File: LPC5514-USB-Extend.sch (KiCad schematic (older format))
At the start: 5 parts

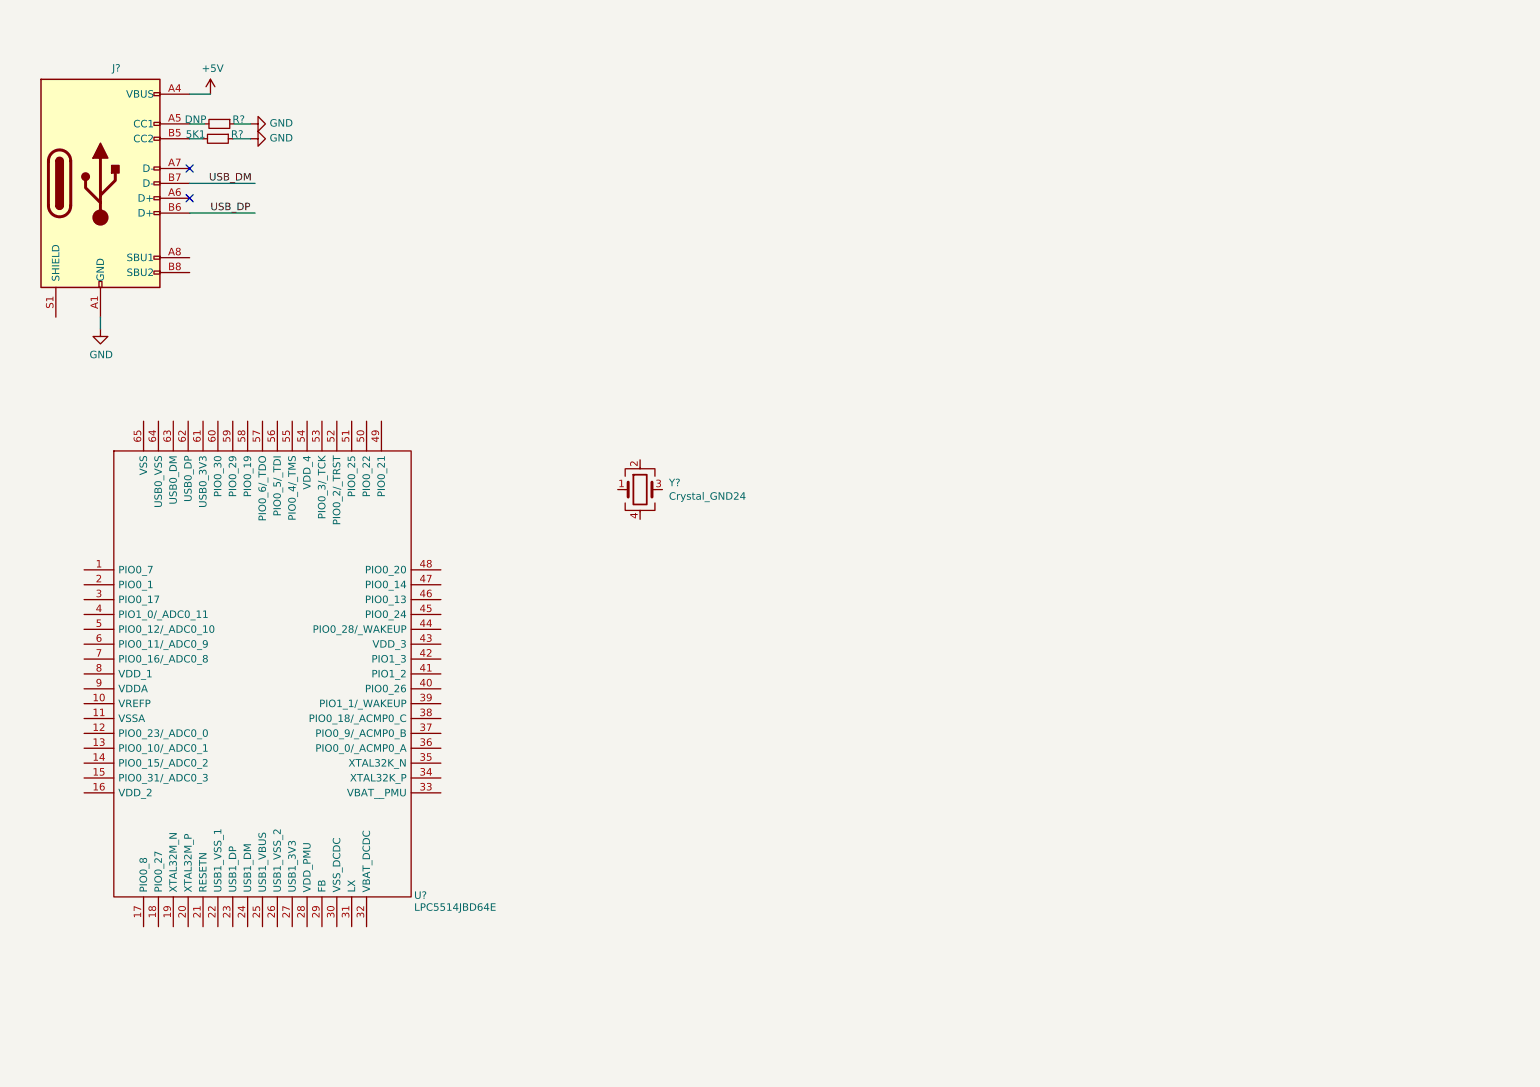
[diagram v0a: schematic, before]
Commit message: update design, usb0/1 connection & power
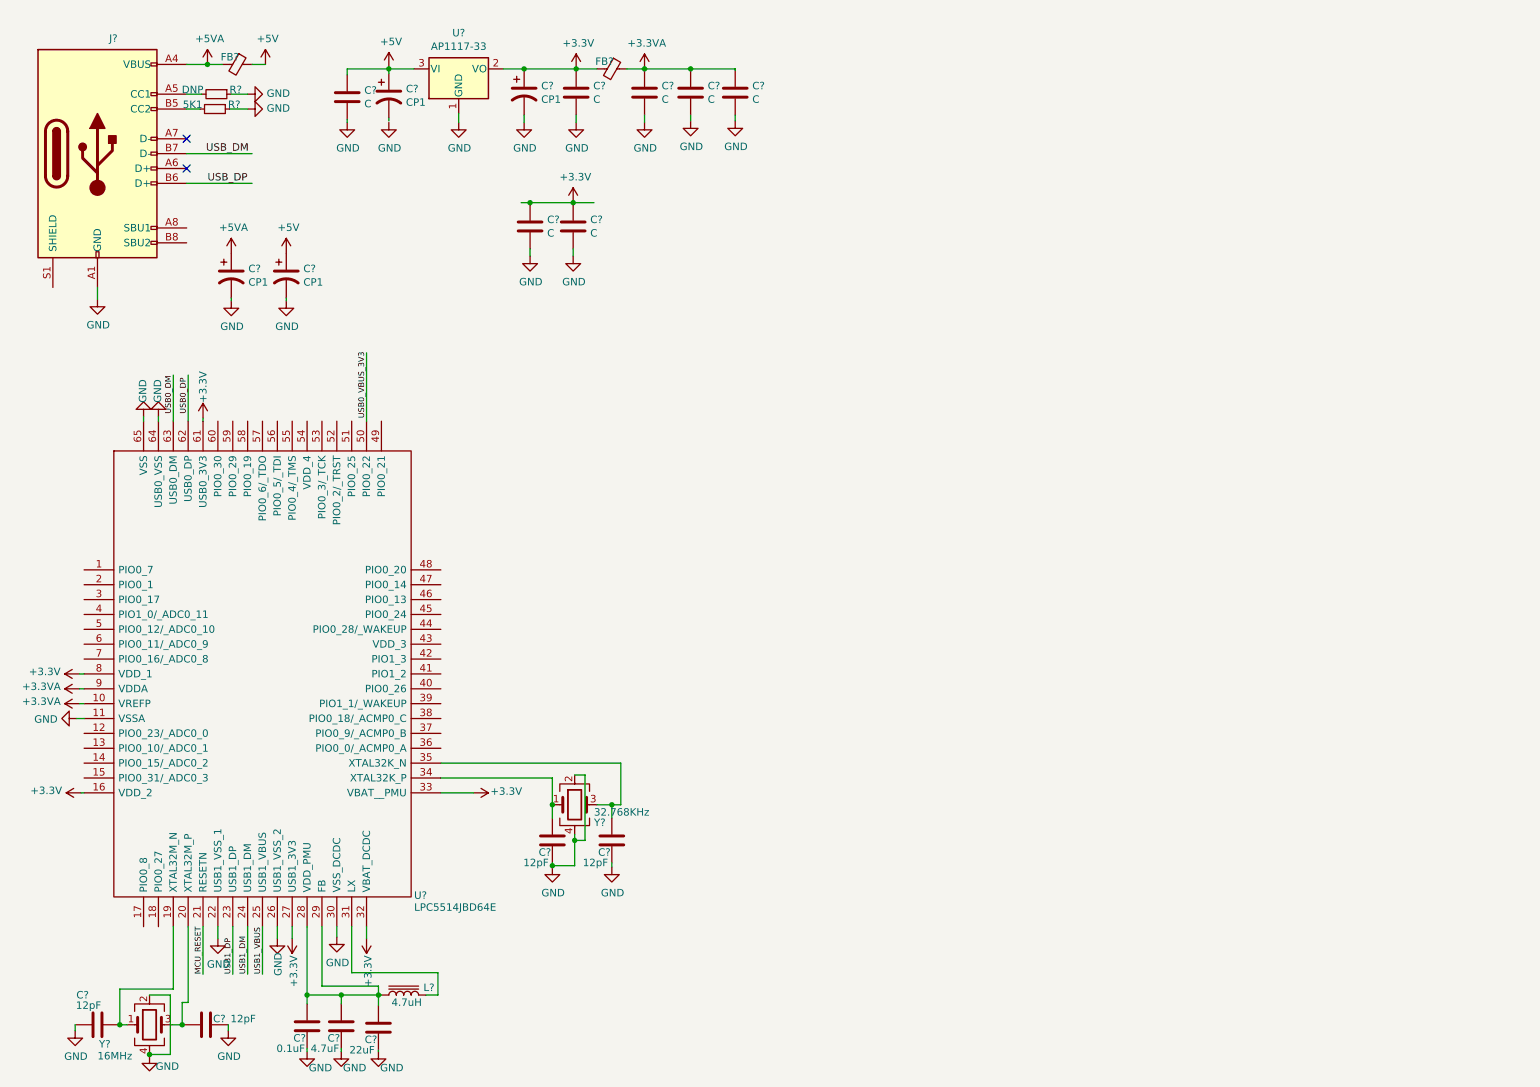
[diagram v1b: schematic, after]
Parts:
- added C? (x4): CP1, symbol Device:CP1
- added C? (x7): C, symbol Device:C
- added C? (x4): 12pF, symbol Device:C
- added C?: 0.1uF, symbol Device:C
- added C?: 4.7uF, symbol Device:C
- added C?: 22uF, symbol Device:C
- added FB? (x2): Ferrite_Bead_Small, symbol Device:Ferrite_Bead_Small
- added L?: 4.7uH, symbol Device:L_Core_Iron
- added U?: AP1117-33, Package_TO_SOT_SMD:SOT-223-3_TabPin2, symbol Regulator_Linear:AP1117-33
- added Y?: 32.768KHz, symbol Device:Crystal_GND24
- Y?: value Crystal_GND24 -> 16MHz
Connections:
- net labels added: +3.3V, +3.3VA, +5VA, MCU_RESET, USB0_DM, USB0_DP, USB0_VBUS_3V3, USB1_DM, USB1_DP, USB1_VBUS
- wire segments 8 -> 113
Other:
- moved on the sheet: J?, R?, Y?

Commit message: update sch and add footprint
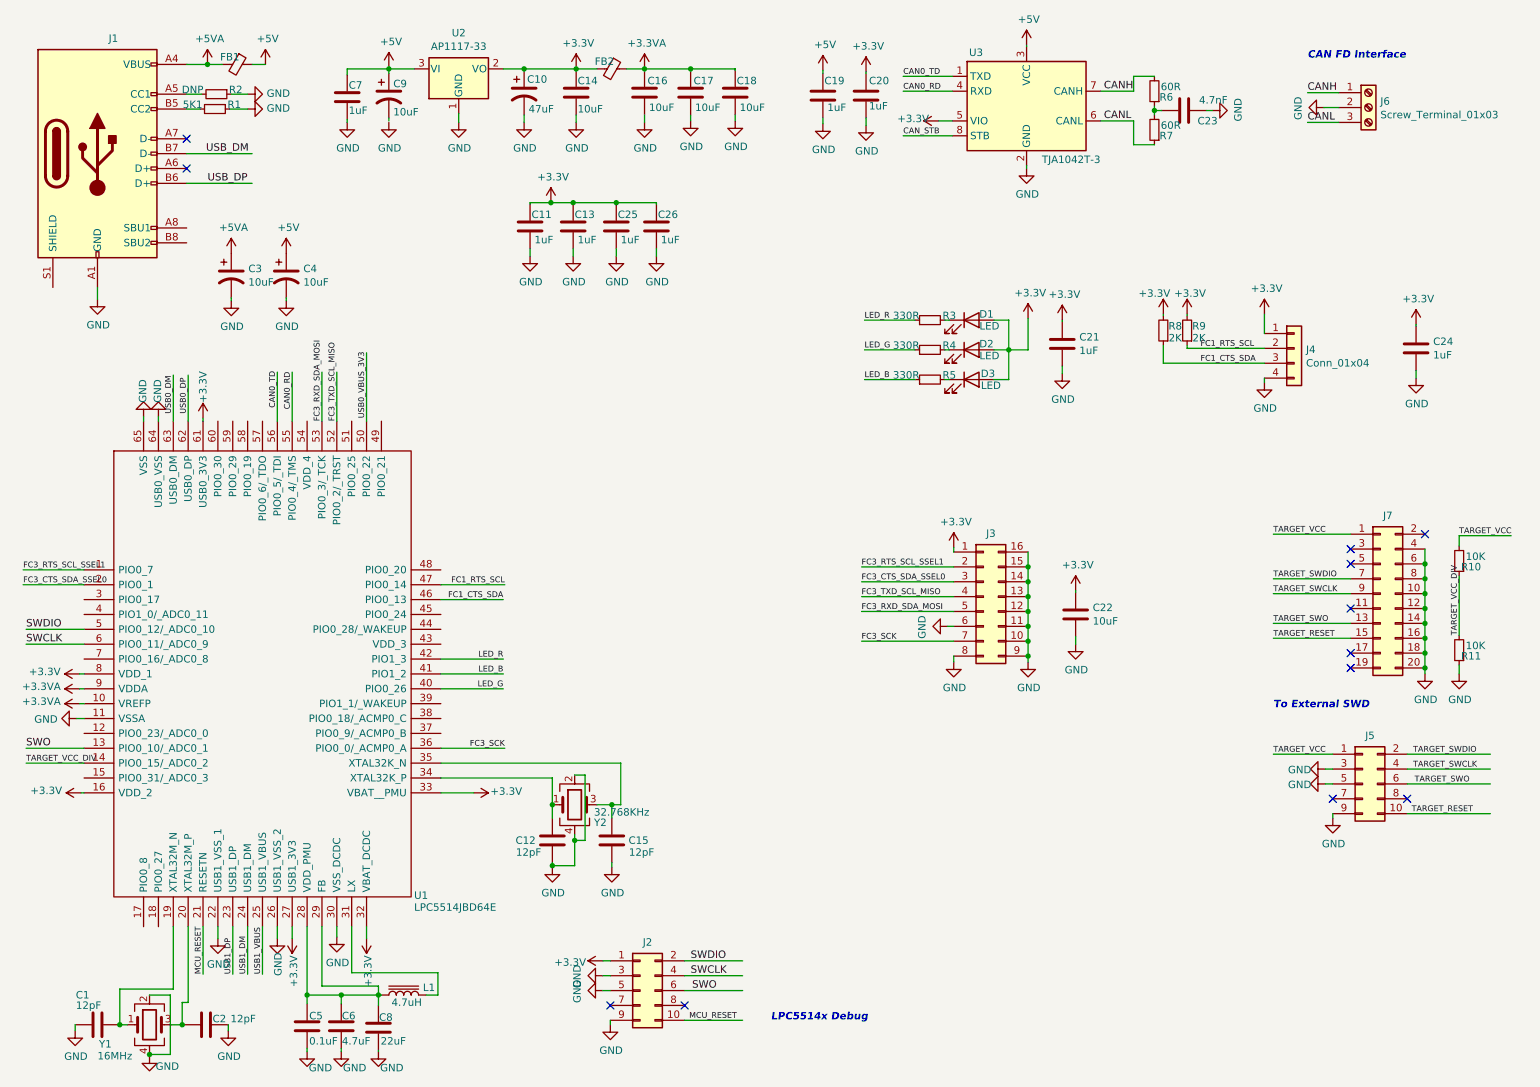
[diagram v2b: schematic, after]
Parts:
- added C19, C20, C24, C25, C26: 1uF, Capacitor_SMD:C_0603_1608Metric_Pad1.08x0.95mm_HandSolder, symbol Device:C
- added C21: 1uF, Capacitor_SMD:C_0805_2012Metric_Pad1.18x1.45mm_HandSolder, symbol Device:C
- added C22: 10uF, Capacitor_SMD:C_0603_1608Metric_Pad1.08x0.95mm_HandSolder, symbol Device:C
- added C23: 4.7nF, Capacitor_SMD:C_0603_1608Metric_Pad1.08x0.95mm_HandSolder, symbol Device:C
- added D1, D2, D3: LED, LED_SMD:LED_0603_1608Metric, symbol Device:LED
- added J2, J5: Conn_02x05_Odd_Even, Connector_PinHeader_1.27mm:PinHeader_2x05_P1.27mm_Vertical, symbol Connector_Generic:Conn_02x05_Odd_Even
- added J3: Conn_02x08_Counter_Clockwise, Connector_PinHeader_2.54mm:PinHeader_2x08_P2.54mm_Vertical, symbol Connector_Generic:Conn_02x08_Counter_Clockwise
- added J4: Conn_01x04, Connector_PinHeader_2.54mm:PinHeader_1x04_P2.54mm_Vertical, symbol Connector_Generic:Conn_01x04
- added J6: Screw_Terminal_01x03, Connector_Phoenix_MSTB:PhoenixContact_MSTBA_2,5_3-G-5,08_1x03_P5.08mm_Horizontal, symbol Connector:Screw_Terminal_01x03
- added J7: Conn_02x10_Odd_Even, Connector_PinHeader_2.54mm:PinHeader_2x10_P2.54mm_Vertical, symbol Connector_Generic:Conn_02x10_Odd_Even
- added R10, R11: 10K, Resistor_SMD:R_0603_1608Metric, symbol Device:R_Small
- added R3, R4, R5: 330R, Resistor_SMD:R_0603_1608Metric, symbol Device:R_Small
- added R6, R7: 60R, Resistor_SMD:R_0603_1608Metric, symbol Device:R_Small
- added R8, R9: 2K, Resistor_SMD:R_0603_1608Metric, symbol Device:R_Small
- added U3: TJA1042T-3, Package_SO:SOIC-8_3.9x4.9mm_P1.27mm, symbol Interface_CAN_LIN:TJA1042T-3
- C1, C12, C15, C2, C5: renamed from C?; footprint (none) -> Capacitor_SMD:C_0603_1608Metric_Pad1.08x0.95mm_HandSolder
- C10: renamed from C?; value CP1 -> 47uF; footprint (none) -> Capacitor_SMD:C_0805_2012Metric_Pad1.18x1.45mm_HandSolder
- C11, C13, C7: renamed from C?; value C -> 1uF; footprint (none) -> Capacitor_SMD:C_0603_1608Metric_Pad1.08x0.95mm_HandSolder
- C14, C16, C17, C18: renamed from C?; value C -> 10uF; footprint (none) -> Capacitor_SMD:C_0805_2012Metric_Pad1.18x1.45mm_HandSolder
- C3, C4, C9: renamed from C?; value CP1 -> 10uF; footprint (none) -> Capacitor_SMD:C_0805_2012Metric_Pad1.18x1.45mm_HandSolder
- C6, C8: renamed from C?; footprint (none) -> Capacitor_SMD:C_0805_2012Metric_Pad1.18x1.45mm_HandSolder
- FB1, FB2: renamed from FB?; footprint (none) -> Inductor_SMD:L_0603_1608Metric
- J1: renamed from J?; footprint (none) -> Connector_USB:USB_C_Receptacle_Amphenol_12401548E4-2A
- L1: renamed from L?; footprint (none) -> Resistor_SMD:R_0603_1608Metric
- R1, R2: renamed from R?; footprint (none) -> Resistor_SMD:R_0603_1608Metric
- U1: renamed from U?; footprint QFP50P1200X1200X120-65N -> LPC5514JBD64E:QFP50P1200X1200X120-65N
- Y1, Y2: renamed from Y?; footprint (none) -> Oscillator:Oscillator_SMD_Abracon_ASE-4Pin_3.2x2.5mm
- gave numbers to parts that had none: 1
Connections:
- net labels added: CAN0_RD, CAN0_TD, CANH, CANL, CAN_STB, FC1_CTS_SDA, FC1_RTS_SCL, FC3_CTS_SDA_SSEL0, FC3_RTS_SCL_SSEL1, FC3_RXD_SDA_MOSI, FC3_SCK, FC3_TXD_SCL_MISO, LED_B, LED_G, LED_R, SWCLK, SWDIO, SWO, TARGET_RESET, TARGET_SWCLK, TARGET_SWDIO, TARGET_SWO, TARGET_VCC, TARGET_VCC_DIV
- wire segments 113 -> 234
- no-connect marks 2 -> 12
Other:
- note added: "CAN FD Interface"
- note added: "LPC5514x Debug"
- note added: "To External SWD"

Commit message: update pcb
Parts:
- L1: footprint Resistor_SMD:R_0603_1608Metric -> Inductor_SMD:L_Wuerth_MAPI-2512
- R1: value 5K1 -> DNP
- R2: value DNP -> 5K1
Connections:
- net labels removed: USB_DM, USB_DP
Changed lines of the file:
@@
 P 2230 1180
 F 0 "R2" V 2200 1310 50  0000 C CNN
-F 1 "DNP" V 2200 1020 50  0000 C CNN
+F 1 "5K1" V 2200 1020 50  0000 C CNN
 F 2 "Resistor_SMD:R_0603_1608Metric" H 2230 1180 50  0001 C CNN
 F 3 "~" H 2230 1180 50  0001 C CNN
@@
 P 2220 1280
 F 0 "R1" V 2190 1410 50  0000 C CNN
-F 1 "5K1" V 2190 1130 50  0000 C CNN
+F 1 "DNP" V 2190 1130 50  0000 C CNN
 F 2 "Resistor_SMD:R_0603_1608Metric" H 2220 1280 50  0001 C CNN
 F 3 "~" H 2220 1280 50  0001 C CNN
@@
 Wire Wire Line
 	2330 1180 2440 1180
-NoConn ~ 2030 1480
-NoConn ~ 2030 1680
-Wire Wire Line
-	2470 1580 2030 1580
-Wire Wire Line
-	2470 1780 2030 1780
-Text Label 2160 1580 0    50   ~ 0
-USB_DM
-Text Label 2170 1780 0    50   ~ 0
-USB_DP
+Wire Wire Line
+	2470 1480 2030 1480
+Wire Wire Line
+	2470 1680 2030 1680
+Text Label 2160 1480 0    50   ~ 0
+USB1_DM
+Text Label 2170 1680 0    50   ~ 0
+USB1_DP
 $Comp
 L power:GND #PWR07
@@
 Wire Wire Line
 	3560 1010 3390 1010
-Wire Wire Line
-	3390 1010 3390 1040
-Wire Wire Line
-	3390 1010 3390 1000
-Connection ~ 3390 1010
 $Comp
 L power:GND #PWR031
@@
 $EndComp
 Wire Wire Line
-	3380 1010 3110 1010
-Wire Wire Line
 	3110 1010 3110 1050
 $Comp
@@
 	1    0    0    -1
 $EndComp
-Connection ~ 4650 1010
 Wire Wire Line
 	4300 1320 4300 1370
@@
 $EndComp
 Wire Wire Line
-	4660 1010 4790 1010
-Wire Wire Line
 	4990 1010 5110 1010
 Wire Wire Line
@@
 F 0 "L1" V 3540 7070 50  0000 C CNN
 F 1 "4.7uH" V 3440 7220 50  0000 C CNN
-F 2 "Resistor_SMD:R_0603_1608Metric" H 3490 7240 50  0001 C CNN
+F 2 "Inductor_SMD:L_Wuerth_MAPI-2512" H 3490 7240 50  0001 C CNN
 F 3 "~" H 3490 7240 50  0001 C CNN
 	1    3490 7240
@@
 Wire Wire Line
 	9570 1370 9780 1370
+Text Label 9570 1370 0    50   ~ 0
+CANH
 Text Label 9570 1170 0    50   ~ 0
-CANH
-Text Label 9570 1370 0    50   ~ 0
 CANL
 Text Notes 9570 950  0    50   Italic 10
@@
 Wire Wire Line
 	7560 3100 7560 2910
+Wire Wire Line
+	3390 1000 3390 1010
+Wire Wire Line
+	3110 1010 3390 1010
+Connection ~ 3390 1010
+Wire Wire Line
+	3390 1010 3390 1040
+Wire Wire Line
+	4790 1010 4650 1010
+Connection ~ 4650 1010
+NoConn ~ 2030 1580
+NoConn ~ 2030 1780
 $EndSCHEMATC

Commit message: update design
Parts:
- added DNP1: Ferrite_Bead_Small, Inductor_SMD:L_0603_1608Metric, symbol Device:Ferrite_Bead_Small
- added R12: 10K, Resistor_SMD:R_0603_1608Metric, symbol Device:R_Small
- added R13: 20K, Resistor_SMD:R_0603_1608Metric, symbol Device:R_Small
- added TP1, TP2: TestPoint, TestPoint:TestPoint_Pad_1.0x1.0mm, symbol Connector:TestPoint
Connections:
- wire segments 234 -> 245
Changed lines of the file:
@@
 USB0_VBUS_3V3
 Wire Wire Line
-	3240 2920 3240 3380
+	3240 2920 3240 3240
 Text Label 2340 7100 1    39   ~ 0
 USB1_DP
@@
 Text Label 2540 7100 1    39   ~ 0
 USB1_VBUS
-Wire Wire Line
-	2540 6780 2540 7100
 $Comp
 L power:+3.3V #PWR023
@@
 Text Label 4170 5580 2    39   ~ 0
 FC3_SCK
+Text Label 6570 4460 0    39   ~ 0
+FC3_RTS_SCL_SSEL1
 Text Label 6570 4360 0    39   ~ 0
-FC3_RTS_SCL_SSEL1
-Text Label 6570 4460 0    39   ~ 0
 FC3_CTS_SDA_SSEL0
 Wire Wire Line
+	6570 4460 7190 4460
+Wire Wire Line
 	6570 4360 7190 4360
-Wire Wire Line
-	6570 4460 7190 4460
 Text Label 6570 4660 0    39   ~ 0
 FC3_RXD_SDA_MOSI
@@
 $EndComp
 Wire Wire Line
-	7560 2900 7690 2900
-Wire Wire Line
 	7690 2900 7690 2690
 $Comp
@@
 	7560 2700 7560 2900
 Wire Wire Line
-	7460 2900 7560 2900
-Connection ~ 7560 2900
-Wire Wire Line
 	7460 3100 7560 3100
-Wire Wire Line
-	7560 3100 7560 2910
 Wire Wire Line
 	3390 1000 3390 1010
@@
 NoConn ~ 2030 1580
 NoConn ~ 2030 1780
+Text Label 2540 3050 3    39   ~ 0
+CAN_STB
+Wire Wire Line
+	2540 3380 2540 3050
+$Comp
+L Device:Ferrite_Bead_Small DNP1
+U 1 1 60D22786
+P 2410 7260
+F 0 "DNP1" V 2360 7210 50  0000 C CNN
+F 1 "Ferrite_Bead_Small" V 2264 7260 50  0001 C CNN
+F 2 "Inductor_SMD:L_0603_1608Metric" V 2340 7260 50  0001 C CNN
+F 3 "~" H 2410 7260 50  0001 C CNN
+	1    2410 7260
+	0    1    1    0
+$EndComp
+Wire Wire Line
+	2540 7260 2510 7260
+Wire Wire Line
+	2540 6780 2540 7260
+$Comp
+L power:+5VA #PWR0101
+U 1 1 60D379FF
+P 2270 7260
+F 0 "#PWR0101" H 2270 7110 50  0001 C CNN
+F 1 "+5VA" V 2330 7370 50  0000 C CNN
+F 2 "" H 2270 7260 50  0001 C CNN
+F 3 "" H 2270 7260 50  0001 C CNN
+	1    2270 7260
+	0    -1   -1   0
+$EndComp
+Wire Wire Line
+	2270 7260 2310 7260
+$Comp
+L Device:R_Small R12
+U 1 1 60D68422
+P 3940 3280
+F 0 "R12" H 4020 3230 50  0000 C CNN
+F 1 "10K" H 4040 3310 50  0000 C CNN
+F 2 "Resistor_SMD:R_0603_1608Metric" H 3940 3280 50  0001 C CNN
+F 3 "~" H 3940 3280 50  0001 C CNN
+	1    3940 3280
+	1    0    0    -1
+$EndComp
+$Comp
+L Device:R_Small R13
+U 1 1 60D6B3D9
+P 3940 3530
+F 0 "R13" H 4020 3480 50  0000 C CNN
+F 1 "20K" H 4040 3560 50  0000 C CNN
+F 2 "Resistor_SMD:R_0603_1608Metric" H 3940 3530 50  0001 C CNN
+F 3 "~" H 3940 3530 50  0001 C CNN
+	1    3940 3530
+	1    0    0    -1
+$EndComp
+$Comp
+L power:GND #PWR0102
+U 1 1 60D6D367
+P 3940 3660
+F 0 "#PWR0102" H 3940 3410 50  0001 C CNN
+F 1 "GND" H 3945 3487 50  0000 C CNN
+F 2 "" H 3940 3660 50  0001 C CNN
+F 3 "" H 3940 3660 50  0001 C CNN
+	1    3940 3660
+	1    0    0    -1
+$EndComp
+Wire Wire Line
+	3940 3630 3940 3660
+Wire Wire Line
+	3940 3380 3940 3400
+$Comp
+L power:+5V #PWR0103
+U 1 1 60D8D0A9
+P 3940 3140
+F 0 "#PWR0103" H 3940 2990 50  0001 C CNN
+F 1 "+5V" H 3955 3313 50  0000 C CNN
+F 2 "" H 3940 3140 50  0001 C CNN
+F 3 "" H 3940 3140 50  0001 C CNN
+	1    3940 3140
+	1    0    0    -1
+$EndComp
+Wire Wire Line
+	3940 3140 3940 3180
+Wire Wire Line
+	3940 3400 3500 3400
+Wire Wire Line
+	3500 3400 3500 3240
+Wire Wire Line
+	3500 3240 3240 3240
+Connection ~ 3940 3400
+Wire Wire Line
+	3940 3400 3940 3430
+Connection ~ 3240 3240
+Wire Wire Line
+	3240 3240 3240 3380
+$Comp
+L Connector:TestPoint TP1
+U 1 1 60DAF984
+P 1940 3070
+F 0 "TP1" H 1870 3260 50  0000 L CNN
+F 1 "TestPoint" H 1998 3097 50  0001 L CNN
+F 2 "TestPoint:TestPoint_Pad_1.0x1.0mm" H 2140 3070 50  0001 C CNN
+F 3 "~" H 2140 3070 50  0001 C CNN
+	1    1940 3070
+	1    0    0    -1
+$EndComp
+$Comp
+L Connector:TestPoint TP2
+U 1 1 60DB8BF6
+P 2040 3070
+F 0 "TP2" H 1970 3260 50  0000 L CNN
+F 1 "TestPoint" H 2098 3097 50  0001 L CNN
+F 2 "TestPoint:TestPoint_Pad_1.0x1.0mm" H 2240 3070 50  0001 C CNN
+F 3 "~" H 2240 3070 50  0001 C CNN
+	1    2040 3070
+	1    0    0    -1
+$EndComp
+Wire Wire Line
+	7460 2900 7560 2900
+Wire Wire Line
+	7560 3100 7560 2900
+Connection ~ 7560 2900
+Wire Wire Line
+	7560 2900 7690 2900
 $EndSCHEMATC

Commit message: update pcb & add data manual
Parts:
- J1: footprint Connector_USB:USB_C_Receptacle_Amphenol_12401548E4-2A -> Connector_USB:USB_C_Receptacle_HRO_TYPE-C-31-M-12; PN_JLC (none) -> TYPE-C-31-M-12
- U2: PN_JLC (none) -> AP1117E33G-13
- U3: PN_JLC (none) -> TJA1042T/3/1J
- Y1: PN_JLC (none) -> C521588
- Y2: PN_JLC (none) -> C117875
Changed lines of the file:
@@
 F 1 "16MHz" H 1430 7230 50  0000 L CNN
 F 2 "Oscillator:Oscillator_SMD_Abracon_ASE-4Pin_3.2x2.5mm" H 1780 7440 50  0001 C CNN
-F 3 "~" H 1780 7440 50  0001 C CNN
+F 3 "https://atta.szlcsc.com/upload/public/pdf/source/20171013/C124322_15078985210081032928.pdf" H 1780 7440 50  0001 C CNN
+F 4 "C521588" H 1780 7440 50  0001 C CNN "PN_JLC"
 	1    1780 7440
 	1    0    0    -1
@@
 F 0 "J1" H 1537 2355 50  0000 C CNN
 F 1 "USB_C_Receptacle_USB2.0" H 1537 2356 50  0001 C CNN
-F 2 "Connector_USB:USB_C_Receptacle_Amphenol_12401548E4-2A" H 1580 1580 50  0001 C CNN
+F 2 "Connector_USB:USB_C_Receptacle_HRO_TYPE-C-31-M-12" H 1580 1580 50  0001 C CNN
 F 3 "https://www.usb.org/sites/default/files/documents/usb_type-c.zip" H 1580 1580 50  0001 C CNN
+F 4 "TYPE-C-31-M-12" H 1430 1580 50  0001 C CNN "PN_JLC"
 	1    1430 1580
 	1    0    0    -1
@@
 F 2 "Package_TO_SOT_SMD:SOT-223-3_TabPin2" H 3860 1210 50  0001 C CNN
 F 3 "http://www.diodes.com/datasheets/AP1117.pdf" H 3960 760 50  0001 C CNN
+F 4 "AP1117E33G-13" H 3860 1010 50  0001 C CNN "PN_JLC"
 	1    3860 1010
 	1    0    0    -1
@@
 F 1 "32.768KHz" H 4770 5910 50  0000 L CNN
 F 2 "Oscillator:Oscillator_SMD_Abracon_ASE-4Pin_3.2x2.5mm" H 4640 5960 50  0001 C CNN
-F 3 "~" H 4640 5960 50  0001 C CNN
+F 3 "https://atta.szlcsc.com/upload/public/pdf/source/20171013/C124322_15078985210081032928.pdf" H 4640 5960 50  0001 C CNN
+F 4 "C117875" H 4640 5960 50  0001 C CNN "PN_JLC"
 	1    4640 5960
 	1    0    0    -1
@@
 F 2 "Package_SO:SOIC-8_3.9x4.9mm_P1.27mm" H 7680 760 50  0001 C CIN
 F 3 "http://www.nxp.com/documents/data_sheet/TJA1042.pdf" H 7680 1260 50  0001 C CNN
+F 4 "TJA1042T/3/1J" H 7680 1260 50  0001 C CNN "PN_JLC"
 	1    7680 1260
 	1    0    0    -1
